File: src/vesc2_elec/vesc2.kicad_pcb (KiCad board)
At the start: 6 copper layers, 36 x 57 mm, 120 parts, among them J101 XT-30-TOP, J102 HALL/ENCODER, J103 SM02B-PASS, J104 IDC6, J105 MR_60_TOP, Q301 IRFH7440TRPBF, Q302 IRFH7440TRPBF, Q401 IRFH7440TRPBF, Q402 IRFH7440TRPBF, Q501 IRFH7440TRPBF, Q502 IRFH7440TRPBF, U101 STM32G474_VESC, U102 TCAN1462V, U103 HX4002, U201 DRV8301, Y101 24Mhz

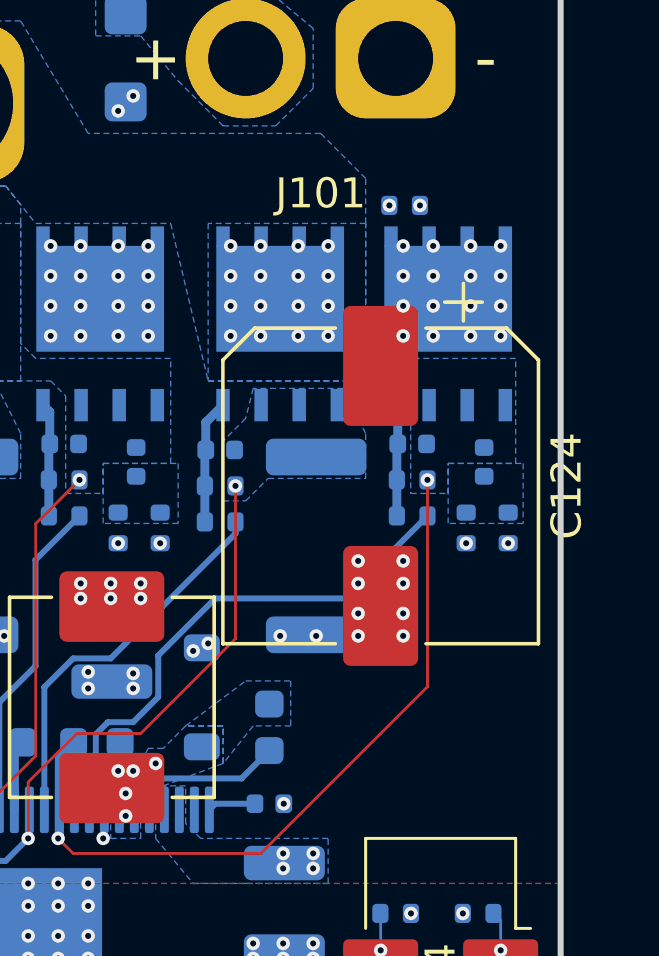
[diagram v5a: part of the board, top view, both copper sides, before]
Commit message: Changes to power zones and mosfet inputs
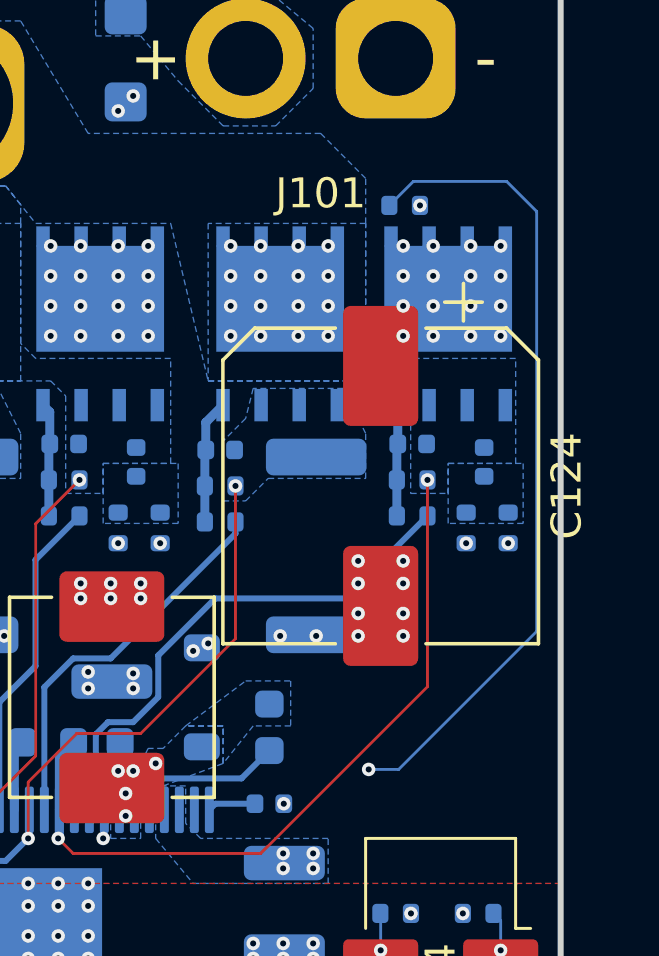
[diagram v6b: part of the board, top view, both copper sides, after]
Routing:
- net Net-(U101A-PA3_TMP_BRD): track 43.3 -> 51.7 mm
- added copper zone on In2.Cu, net /PHASEA
- added copper zone on In2.Cu, net /PHASEB
- added copper zone on In2.Cu, net /PHASEC
- added copper zone on In2.Cu, net VBUS
- added copper zone on In3.Cu, net VBUS
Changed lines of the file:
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@@
 	)
 	(via
-		(at 193.290001 83.4)
+		(at 186.75 116.25)
 		(size 0.45)
 		(drill 0.2)
@@
 	)
 	(via
-		(at 186.75 116.25)
+		(at 192.6 102.2)
 		(size 0.45)
 		(drill 0.2)
@@
 	)
 	(segment
+		(start 197.2 82.6)
+		(end 198.2 83.6)
+		(width 0.095)
+		(layer "B.Cu")
+		(net 2)
+	)
+	(segment
+		(start 194.090001 82.6)
+		(end 197.2 82.6)
+		(width 0.095)
+		(layer "B.Cu")
+		(net 2)
+	)
+	(segment
 		(start 186.675001 117.25)
 		(end 186.750001 117.325)
@@
 	)
 	(segment
+		(start 193.6 102.2)
+		(end 192.6 102.2)
+		(width 0.095)
+		(layer "B.Cu")
+		(net 2)
+	)
+	(segment
 		(start 183.275 118)
 		(end 184.025 117.25)
@@
 	)
 	(segment
+		(start 198.2 97.6)
+		(end 193.6 102.2)
+		(width 0.095)
+		(layer "B.Cu")
+		(net 2)
+	)
+	(segment
+		(start 198.2 83.6)
+		(end 198.2 97.6)
+		(width 0.095)
+		(layer "B.Cu")
+		(net 2)
+	)
+	(segment
 		(start 186.75 116.25)
 		(end 186.75 117.324999)
@@
 	)
 	(segment
-		(start 180.759999 117.5)
-		(end 181.259999 118)
-		(width 0.2)
+		(start 193.290001 83.4)
+		(end 194.090001 82.6)
+		(width 0.095)
 		(layer "B.Cu")
 		(net 2)
 	)
 	(segment
-		(start 193.1 83.4)
-		(end 191.75 84.75)
-		(width 0.095)
-		(layer "In3.Cu")
+		(start 180.759999 117.5)
+		(end 181.259999 118)
+		(width 0.2)
+		(layer "B.Cu")
 		(net 2)
 	)
 	(segment
-		(start 191.75 84.75)
-		(end 191.75 102.25)
+		(start 191.8 102.2)
+		(end 192.6 102.2)
 		(width 0.095)
 		(layer "In3.Cu")
@@
 	)
 	(segment
-		(start 193.290001 83.4)
-		(end 193.1 83.4)
+		(start 191.75 102.25)
+		(end 191.8 102.2)
 		(width 0.095)
 		(layer "In3.Cu")
@@
 	)
 	(segment
-		(start 193 88.5)
-		(end 193 102)
+		(start 191.5 118.228862)
+		(end 191.3815 118.347362)
 		(width 0.095)
 		(layer "In3.Cu")
@@
 	)
 	(segment
-		(start 191.5 118.228862)
-		(end 191.3815 118.347362)
+		(start 193 88.5)
+		(end 193 103.2)
 		(width 0.095)
 		(layer "In3.Cu")
@@
 	)
 	(segment
-		(start 185.240001 123.75)
-		(end 180.740001 119.25)
+		(start 188 123.75)
+		(end 185.240001 123.75)
 		(width 0.095)
 		(layer "In3.Cu")
@@
 	)
 	(segment
-		(start 191.3815 118.347362)
-		(end 191.3815 118.652638)
+		(start 185.240001 123.75)
+		(end 180.740001 119.25)
 		(width 0.095)
 		(layer "In3.Cu")
@@
 	)
 	(segment
-		(start 191.5 103.5)
-		(end 191.5 118.228862)
+		(start 191.5 120.25)
+		(end 188 123.75)
 		(width 0.095)
 		(layer "In3.Cu")
@@
 	)
 	(segment
-		(start 188 123.75)
-		(end 185.240001 123.75)
+		(start 191.5 118.771138)
+		(end 191.5 120.25)
 		(width 0.095)
 		(layer "In3.Cu")
@@
 	)
 	(segment
-		(start 191.5 120.25)
-		(end 188 123.75)
+		(start 191.5 104.7)
+		(end 191.5 118.228862)
 		(width 0.095)
 		(layer "In3.Cu")
@@
 	)
 	(segment
-		(start 193 102)
-		(end 191.5 103.5)
+		(start 193.75 87.75)
+		(end 193 88.5)
 		(width 0.095)
 		(layer "In3.Cu")
@@
 	)
 	(segment
-		(start 193.75 87.75)
-		(end 193 88.5)
+		(start 193 103.2)
+		(end 191.5 104.7)
 		(width 0.095)
 		(layer "In3.Cu")
@@
 	)
 	(segment
-		(start 191.5 118.771138)
-		(end 191.5 120.25)
+		(start 191.3815 118.347362)
+		(end 191.3815 118.652638)
 		(width 0.095)
 		(layer "In3.Cu")
@@
 		(net 26)
 		(net_name "/PHASEA")
-		(layers "B.Cu" "In3.Cu")
+		(layers "B.Cu" "In2.Cu" "In3.Cu")
 		(hatch edge 0.5)
 		(priority 6)
@@
 		(net 28)
 		(net_name "/PHASEB")
-		(layers "B.Cu" "In3.Cu")
+		(layers "B.Cu" "In2.Cu" "In3.Cu")
 		(hatch edge 0.5)
 		(priority 5)
@@
 		(net 39)
 		(net_name "/PHASEC")
-		(layers "B.Cu" "In3.Cu")
+		(layers "B.Cu" "In2.Cu" "In3.Cu")
 		(hatch edge 0.5)
 		(priority 4)
@@
 		(hatch edge 0.5)
 		(connect_pads
-			(clearance 0.5)
+			(clearance 0.1)
 		)
 		(min_thickness 0.25)
@@
 			)
 		)
+	)
+	(zone
+		(net 108)
+		(net_name "VBUS")
+		(layers "In2.Cu" "In3.Cu")
+		(hatch edge 0.5)
+		(connect_pads yes
+			(clearance 0.2)
+		)
+		(min_thickness 0.25)
+		(filled_areas_thickness no)
+		(fill yes
+			(thermal_gap 0.5)
+			(thermal_bridge_width 0.5)
+		)
+		(polygon
+			(pts
+				(xy 163 75) (xy 163 93) (xy 199 93) (xy 199 75)
+			)
+		)

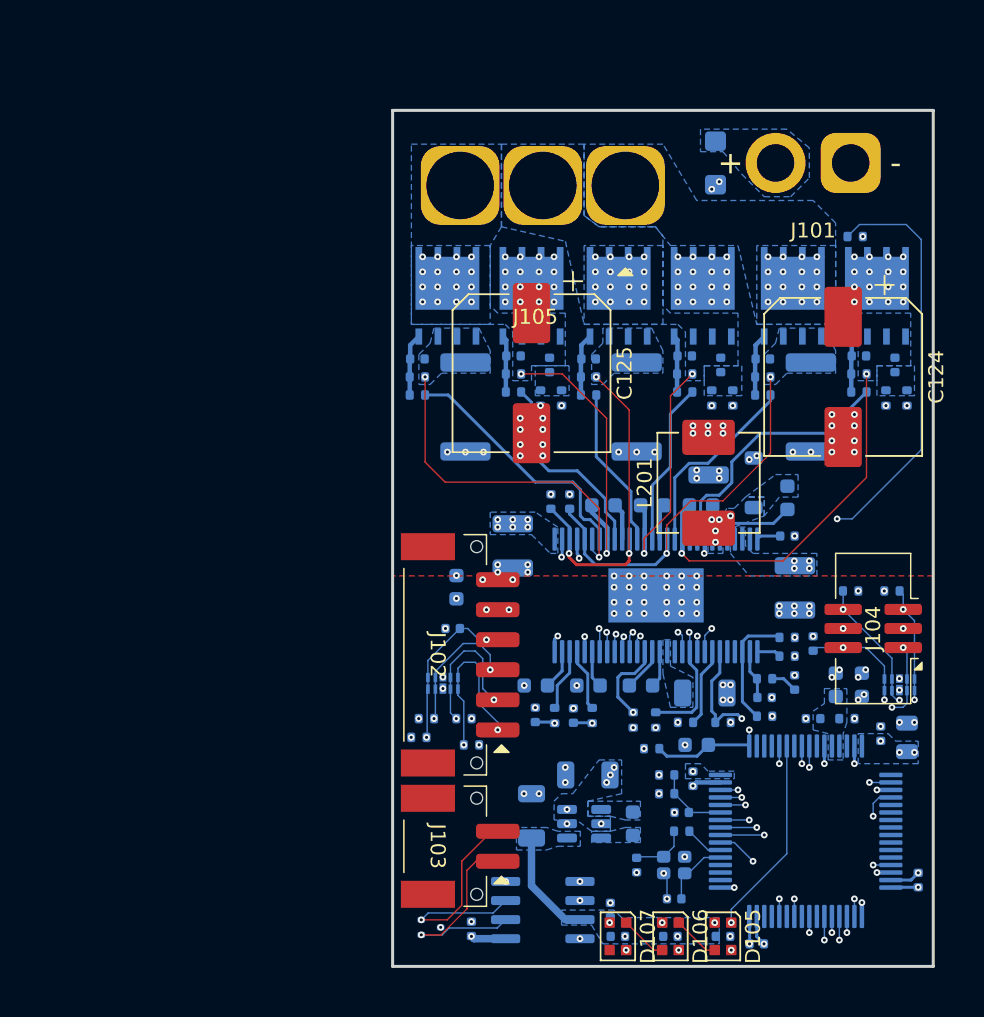
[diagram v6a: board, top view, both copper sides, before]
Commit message: Fix silkscreen and fix zones and DRC pass
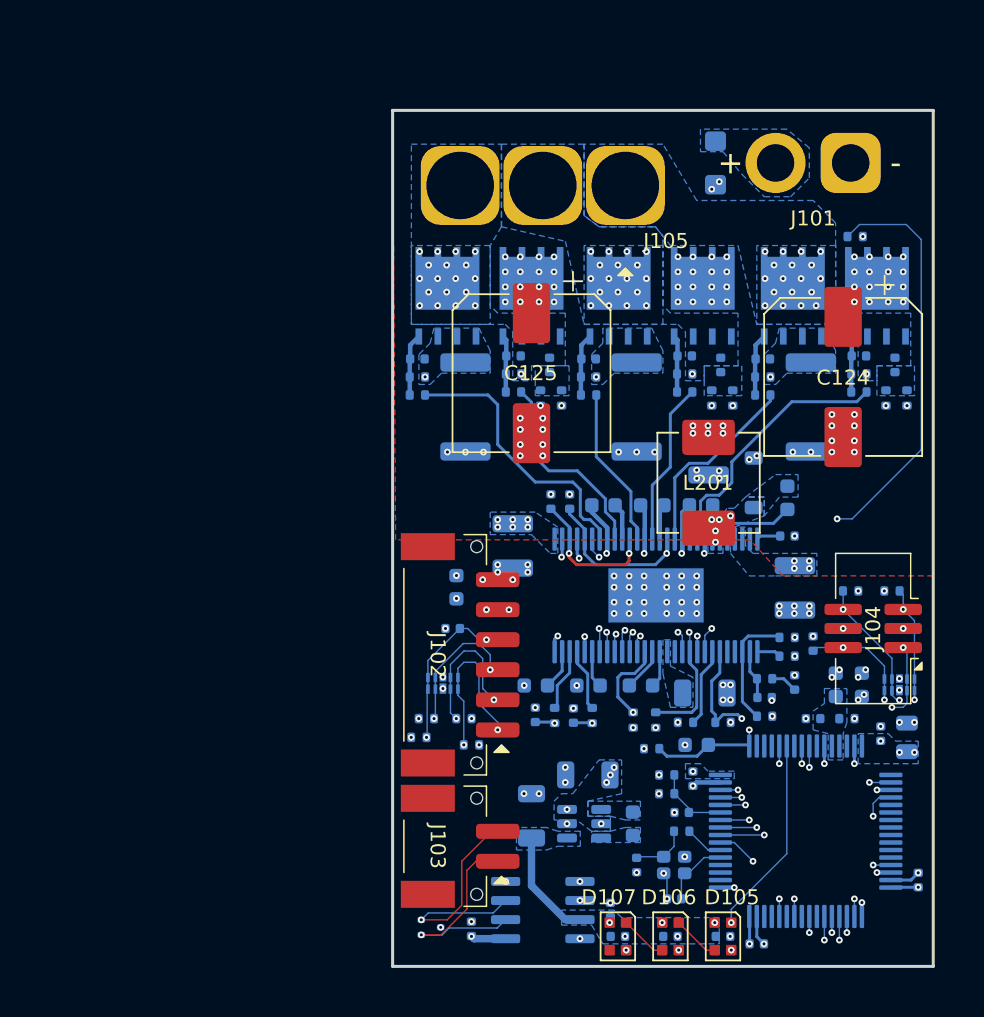
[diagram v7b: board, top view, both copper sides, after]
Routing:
- net VBUS: track 47.6 -> 50.0 mm
- net /Gate Driver/GL_C: track 17.0 -> 18.6 mm
- net SNA: track 26.3 -> 27.4 mm
- net /Gate Driver/H2: track 20.9 -> 21.8 mm
- net /PHASEA: track 25.1 -> 25.8 mm, vias 18 -> 20
- net /Gate Driver/SDO: track 35.6 -> 36.3 mm
- net /PHASEC: track 19.6 -> 19.5 mm, vias 18 -> 20
- net /PHASEB: vias 18 -> 20

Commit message: Add mounting holes to corners of board
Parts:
- added H1: MountingHole, Bluesat:M2.5_Edge, F.Cu at (199.0, 71.0)
- added H2: MountingHole, Bluesat:M2.5_Edge, F.Cu at (163.0, 71.0)
- added H3: MountingHole, Bluesat:M2.5_Edge, F.Cu at (163.0, 132.0)
- added H4: MountingHole, Bluesat:M2.5_Edge, F.Cu at (199.0, 132.0)
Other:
- board size 36 x 57 mm -> 36 x 61 mm
